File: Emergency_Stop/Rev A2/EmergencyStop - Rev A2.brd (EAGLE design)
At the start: 55 x 25 mm, 12 parts, among them J3 NC3FBV2-SW, J4 NC3MAV, J5 22-05-7038-03, J6 22-05-7028-02, T1 EXMACHINA-LOGO-NAME

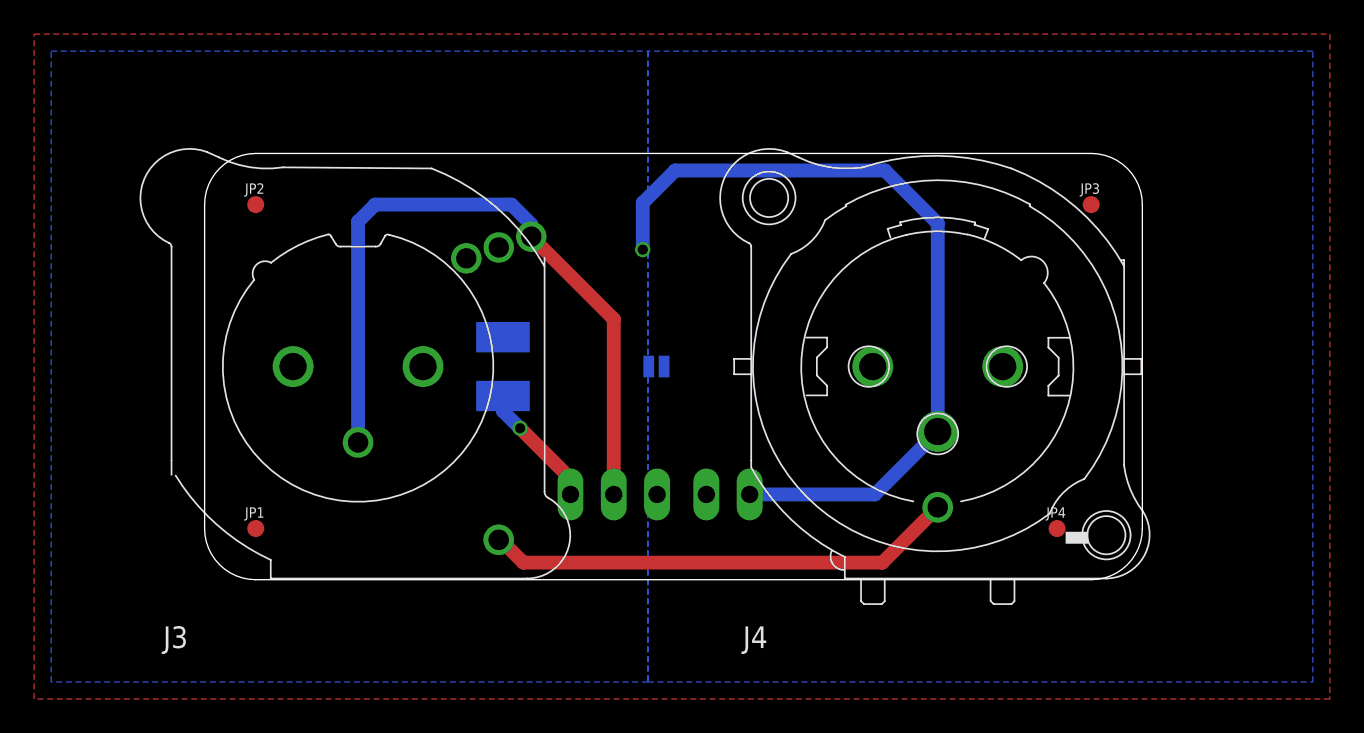
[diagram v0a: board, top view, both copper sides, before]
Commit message: Add MDP files
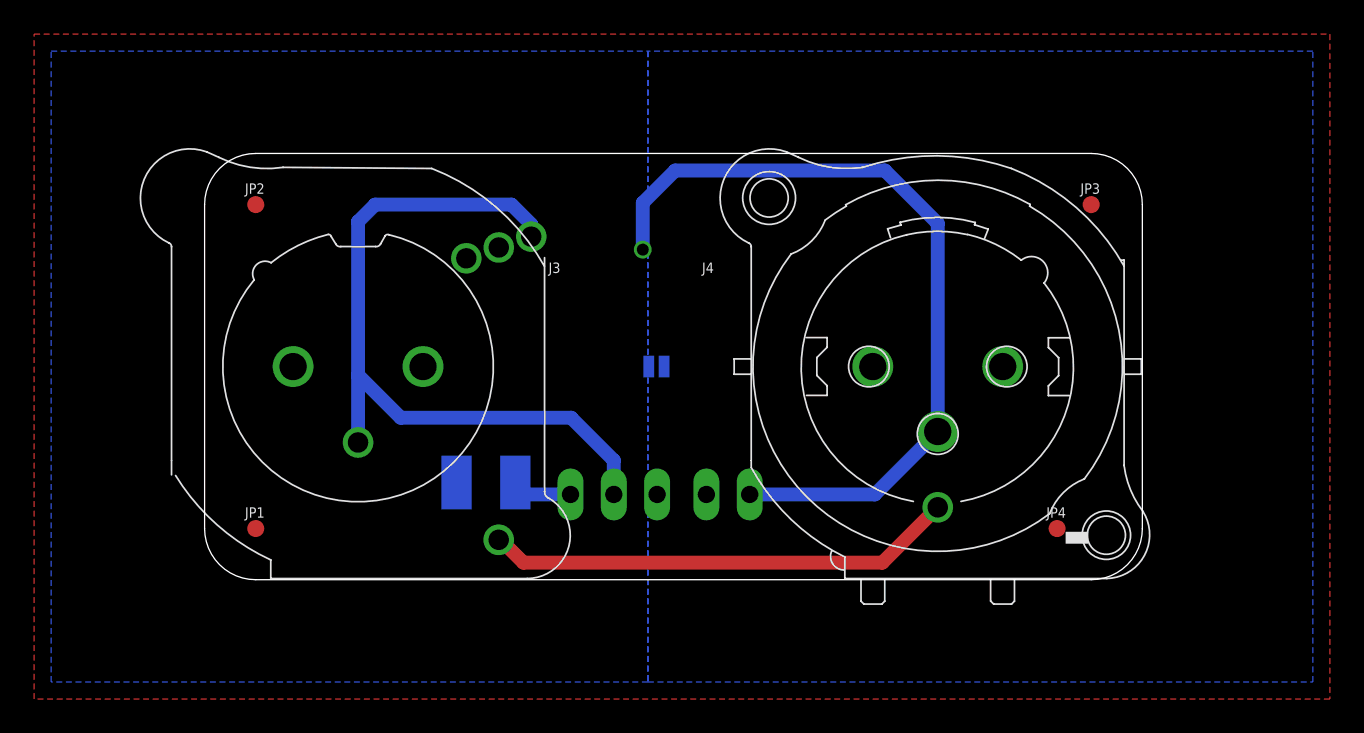
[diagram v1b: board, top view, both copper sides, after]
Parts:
- added U$1: (no value), frames:A4L-LOC
- moved F1 6.87 mm to (16.5, 5.70), turned to 0 degrees
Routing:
- net +24V_IN2: track 7.42 -> 3.52 mm, vias 1 -> 0
- net SIG_IN: track 41.8 -> 43.8 mm
